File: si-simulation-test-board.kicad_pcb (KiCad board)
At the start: 4 copper layers, 50 x 100 mm, 28 parts, among them J1 Conn_SMA_RF2-143-T-17-50-G, J10 Conn_SMA_RF2-143-T-17-50-G, J11 Conn_SMA_RF2-143-T-17-50-G, J12 Conn_SMA_RF2-143-T-17-50-G, J13 Conn_SMA_RF2-143-T-17-50-G, J14 Conn_SMA_RF2-143-T-17-50-G, J15 Conn_SMA_RF2-143-T-17-50-G, J16 Conn_SMA_RF2-143-T-17-50-G, J17 Conn_SMA_RF2-143-T-17-50-G, J18 Conn_SMA_RF2-143-T-17-50-G, J19 Conn_SMA_RF2-143-T-17-50-G, J2 Conn_SMA_RF2-143-T-17-50-G, J20 Conn_SMA_RF2-143-T-17-50-G, J21 Conn_SMA_RF2-143-T-17-50-G, J22 Conn_SMA_RF2-143-T-17-50-G, J3 Conn_SMA_RF2-143-T-17-50-G, J4 Conn_SMA_RF2-143-T-17-50-G, J5 Conn_SMA_RF2-143-T-17-50-G, J6 Conn_SMA_RF2-143-T-17-50-G, J7 Conn_SMA_RF2-143-T-17-50-G, J8 Conn_SMA_RF2-143-T-17-50-G, J9 Conn_SMA_RF2-143-T-17-50-G

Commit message: Finish PCB
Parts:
- moved G*** 1.63 mm to (126.4, 102.0)
- moved C1 1.62 mm to (126.6, 146.3)
- moved J15 1.62 mm to (94.2, 137.6)
- moved J16 1.62 mm to (94.2, 147.6)
- moved J17 1.62 mm to (143.8, 137.6)
- moved J18 1.62 mm to (143.8, 147.6)
- moved J19 1.61 mm to (94.2, 127.6)
- moved J20 1.61 mm to (143.9, 127.6)
- moved C2 1.61 mm to (112.4, 146.4)
- moved J12 1.30 mm to (94.2, 117.3)
- moved J14 1.30 mm to (143.8, 117.3)
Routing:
- net /DIFF_N: track 54.2 -> 55.4 mm
- net /DIFF_P: track 54.2 -> 55.4 mm
- net GND: vias 252 -> 247
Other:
- board text added: "4GHz ANTENNA"
- board text added: "4GHz PATH ANTENNA"
- board text added: "50Ω"
- board text added: "BANDPASS 3.5-4 GHz"
- board text added: "DIFF PAIR/ COUPLER"
- board text added: "LAYER CHANGE"
- board text added: "LONG STUB"
- board text added: "LOOSE MEANDER"
- board text added: "OPEN"
- board text added: "PASS"
- board text added: "PCB SHA ########"
- board text added: "SHORT"
- board text added: "SHORT STUB"
- board text added: "SI test board Rev. 1.0.0"
- board text added: "THIGHT MEANDER"

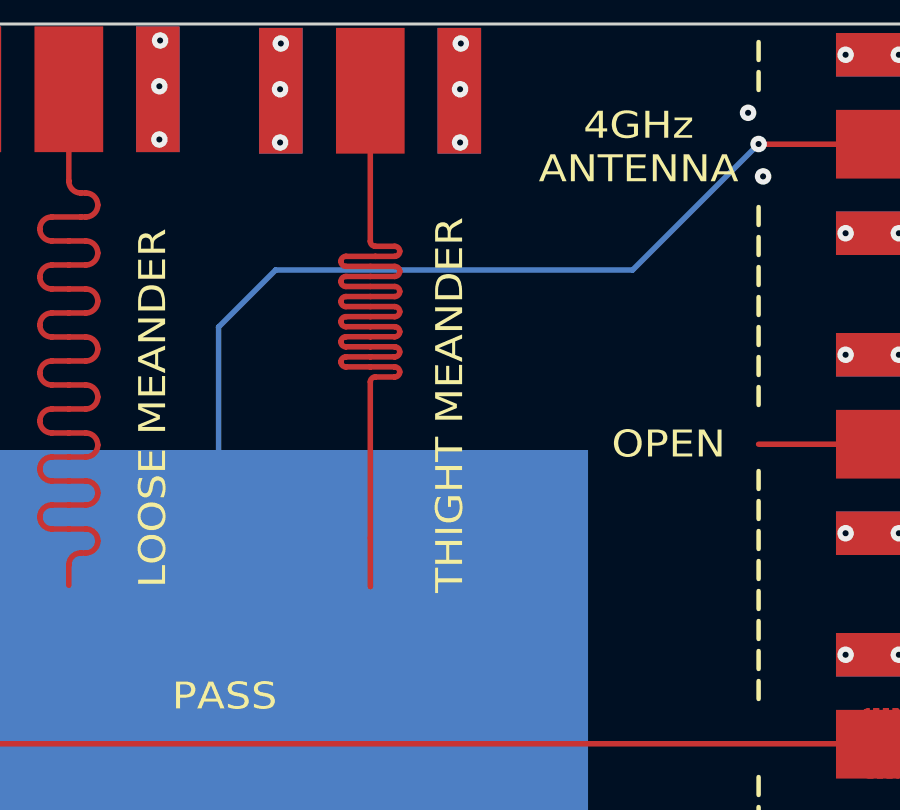
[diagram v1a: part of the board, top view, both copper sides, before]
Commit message: Correct silkscreen 'tight meander' text
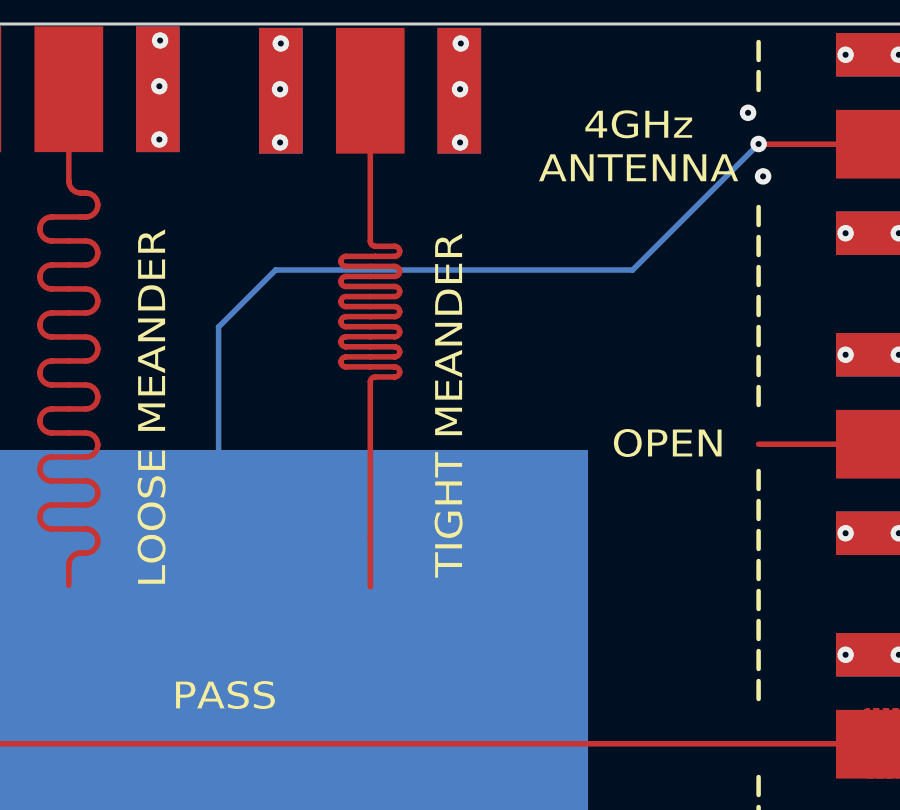
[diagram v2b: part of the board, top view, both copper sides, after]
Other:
- board text added: "TIGHT MEANDER"
- board text removed: "THIGHT MEANDER"
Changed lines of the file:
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@@
     (effects (font (size 0.9 1) (thickness 0.15)))
   )
-  (gr_text "THIGHT MEANDER" (at 126.7 64.7 90) (layer "F.SilkS")
+  (gr_text "TIGHT MEANDER" (at 126.7 64.7 90) (layer "F.SilkS")
     (effects (font (size 0.9 1) (thickness 0.15)))
   )
@@
     (connect_pads (clearance 0))
     (min_thickness 0.254)
-    (keepout (tracks allowed) (vias allowed) (pads allowed ) (copperpour not_allowed) (footprints allowed))
+    (keepout (tracks allowed) (vias allowed) (pads allowed) (copperpour not_allowed) (footprints allowed))
     (fill (thermal_gap 0.508) (thermal_bridge_width 0.508))
     (polygon
@@
     (connect_pads (clearance 0))
     (min_thickness 0.254)
-    (keepout (tracks allowed) (vias allowed) (pads allowed ) (copperpour not_allowed) (footprints allowed))
+    (keepout (tracks allowed) (vias allowed) (pads allowed) (copperpour not_allowed) (footprints allowed))
     (fill (thermal_gap 0.508) (thermal_bridge_width 0.508))
     (polygon
@@
     (connect_pads (clearance 0))
     (min_thickness 0.254)
-    (keepout (tracks allowed) (vias allowed) (pads allowed ) (copperpour not_allowed) (footprints allowed))
+    (keepout (tracks allowed) (vias allowed) (pads allowed) (copperpour not_allowed) (footprints allowed))
     (fill (thermal_gap 0.508) (thermal_bridge_width 0.508))
     (polygon
@@
     (connect_pads (clearance 0))
     (min_thickness 0.254)
-    (keepout (tracks allowed) (vias allowed) (pads allowed ) (copperpour not_allowed) (footprints allowed))
+    (keepout (tracks allowed) (vias allowed) (pads allowed) (copperpour not_allowed) (footprints allowed))
     (fill (thermal_gap 0.508) (thermal_bridge_width 0.508))
     (polygon
@@
     (connect_pads (clearance 0))
     (min_thickness 0.254)
-    (keepout (tracks allowed) (vias allowed) (pads allowed ) (copperpour not_allowed) (footprints allowed))
+    (keepout (tracks allowed) (vias allowed) (pads allowed) (copperpour not_allowed) (footprints allowed))
     (fill (thermal_gap 0.508) (thermal_bridge_width 0.508))
     (polygon
@@
     (connect_pads (clearance 0))
     (min_thickness 0.254)
-    (keepout (tracks allowed) (vias allowed) (pads allowed ) (copperpour not_allowed) (footprints allowed))
+    (keepout (tracks allowed) (vias allowed) (pads allowed) (copperpour not_allowed) (footprints allowed))
     (fill (thermal_gap 0.508) (thermal_bridge_width 0.508))
     (polygon
@@
     (connect_pads (clearance 0))
     (min_thickness 0.254)
-    (keepout (tracks allowed) (vias allowed) (pads allowed ) (copperpour not_allowed) (footprints allowed))
+    (keepout (tracks allowed) (vias allowed) (pads allowed) (copperpour not_allowed) (footprints allowed))
     (fill (thermal_gap 0.508) (thermal_bridge_width 0.508))
     (polygon
@@
     (connect_pads (clearance 0))
     (min_thickness 0.254)
-    (keepout (tracks allowed) (vias allowed) (pads allowed ) (copperpour not_allowed) (footprints allowed))
+    (keepout (tracks allowed) (vias allowed) (pads allowed) (copperpour not_allowed) (footprints allowed))
     (fill (thermal_gap 0.508) (thermal_bridge_width 0.508))
     (polygon
@@
     (connect_pads (clearance 0))
     (min_thickness 0.254)
-    (keepout (tracks allowed) (vias allowed) (pads allowed ) (copperpour not_allowed) (footprints allowed))
+    (keepout (tracks allowed) (vias allowed) (pads allowed) (copperpour not_allowed) (footprints allowed))
     (fill (thermal_gap 0.508) (thermal_bridge_width 0.508))
     (polygon
@@
     (connect_pads (clearance 0))
     (min_thickness 0.254)
-    (keepout (tracks allowed) (vias allowed) (pads allowed ) (copperpour not_allowed) (footprints allowed))
+    (keepout (tracks allowed) (vias allowed) (pads allowed) (copperpour not_allowed) (footprints allowed))
     (fill (thermal_gap 0.508) (thermal_bridge_width 0.508))
     (polygon
@@
     (connect_pads (clearance 0))
     (min_thickness 0.254)
-    (keepout (tracks allowed) (vias allowed) (pads allowed ) (copperpour not_allowed) (footprints allowed))
+    (keepout (tracks allowed) (vias allowed) (pads allowed) (copperpour not_allowed) (footprints allowed))
     (fill (thermal_gap 0.508) (thermal_bridge_width 0.508))
     (polygon
@@
     (connect_pads (clearance 0))
     (min_thickness 0.254)
-    (keepout (tracks allowed) (vias allowed) (pads allowed ) (copperpour not_allowed) (footprints allowed))
+    (keepout (tracks allowed) (vias allowed) (pads allowed) (copperpour not_allowed) (footprints allowed))
     (fill (thermal_gap 0.508) (thermal_bridge_width 0.508))
     (polygon
@@
     (connect_pads (clearance 0))
     (min_thickness 0.254)
-    (keepout (tracks allowed) (vias allowed) (pads allowed ) (copperpour not_allowed) (footprints allowed))
+    (keepout (tracks allowed) (vias allowed) (pads allowed) (copperpour not_allowed) (footprints allowed))
     (fill (thermal_gap 0.508) (thermal_bridge_width 0.508))
     (polygon
@@
     (connect_pads (clearance 0))
     (min_thickness 0.254)
-    (keepout (tracks allowed) (vias allowed) (pads allowed ) (copperpour not_allowed) (footprints allowed))
+    (keepout (tracks allowed) (vias allowed) (pads allowed) (copperpour not_allowed) (footprints allowed))
     (fill (thermal_gap 0.508) (thermal_bridge_width 0.508))
     (polygon
@@
     (connect_pads (clearance 0))
     (min_thickness 0.254)
-    (keepout (tracks allowed) (vias allowed) (pads allowed ) (copperpour not_allowed) (footprints allowed))
+    (keepout (tracks allowed) (vias allowed) (pads allowed) (copperpour not_allowed) (footprints allowed))
     (fill (thermal_gap 0.508) (thermal_bridge_width 0.508))
     (polygon
@@
     (connect_pads (clearance 0))
     (min_thickness 0.254)
-    (keepout (tracks allowed) (vias allowed) (pads allowed ) (copperpour not_allowed) (footprints allowed))
+    (keepout (tracks allowed) (vias allowed) (pads allowed) (copperpour not_allowed) (footprints allowed))
     (fill (thermal_gap 0.508) (thermal_bridge_width 0.508))
     (polygon
@@
     (connect_pads (clearance 0))
     (min_thickness 0.254)
-    (keepout (tracks allowed) (vias allowed) (pads allowed ) (copperpour not_allowed) (footprints allowed))
+    (keepout (tracks allowed) (vias allowed) (pads allowed) (copperpour not_allowed) (footprints allowed))
     (fill (thermal_gap 0.508) (thermal_bridge_width 0.508))
     (polygon
@@
     (connect_pads (clearance 0))
     (min_thickness 0.254)
-    (keepout (tracks allowed) (vias allowed) (pads allowed ) (copperpour not_allowed) (footprints allowed))
+    (keepout (tracks allowed) (vias allowed) (pads allowed) (copperpour not_allowed) (footprints allowed))
     (fill (thermal_gap 0.508) (thermal_bridge_width 0.508))
     (polygon
@@
     (connect_pads yes (clearance 0))
     (min_thickness 0)
-    (keepout (tracks allowed) (vias allowed) (pads allowed ) (copperpour not_allowed) (footprints allowed))
+    (keepout (tracks allowed) (vias allowed) (pads allowed) (copperpour not_allowed) (footprints allowed))
     (fill (thermal_gap 0.508) (thermal_bridge_width 0.508))
     (polygon
@@
     (connect_pads yes (clearance 0))
     (min_thickness 0)
-    (keepout (tracks allowed) (vias allowed) (pads allowed ) (copperpour not_allowed) (footprints allowed))
+    (keepout (tracks allowed) (vias allowed) (pads allowed) (copperpour not_allowed) (footprints allowed))
     (fill (thermal_gap 0.508) (thermal_bridge_width 0.508))
     (polygon
@@
     (connect_pads yes (clearance 0))
     (min_thickness 0.254)
-    (keepout (tracks allowed) (vias allowed) (pads allowed ) (copperpour not_allowed) (footprints allowed))
+    (keepout (tracks allowed) (vias allowed) (pads allowed) (copperpour not_allowed) (footprints allowed))
     (fill (thermal_gap 0.508) (thermal_bridge_width 0.508))
     (polygon
@@
     (connect_pads yes (clearance 0))
     (min_thickness 0)
-    (keepout (tracks allowed) (vias allowed) (pads allowed ) (copperpour not_allowed) (footprints allowed))
+    (keepout (tracks allowed) (vias allowed) (pads allowed) (copperpour not_allowed) (footprints allowed))
     (fill (thermal_gap 0.508) (thermal_bridge_width 0.508))
     (polygon
@@
     (connect_pads yes (clearance 0))
     (min_thickness 0)
-    (keepout (tracks allowed) (vias allowed) (pads allowed ) (copperpour not_allowed) (footprints allowed))
-    (fill (thermal_gap 0.508) (thermal_bridge_width 0.508))
-    (polygon
+    (keepout (tracks allowed) (vias allowed) (pads allowed) (copperpour not_allowed) (footprints allowed))
+    (fill (thermal_gap 0.508) (thermal_bridge_width 0.508))
+    (polygon
